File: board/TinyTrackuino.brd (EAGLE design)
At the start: 49.5 x 49.5 mm, 16 parts, among them M2 HX1, Q1 PMV20XN, PMV16UN, etc, U1 LM60 int, X1 BU-SMA-V, X2 Vin, X3 LM60 ext, X4 Buzzer

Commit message: Fixing temp sensor silkscreen and gps connector
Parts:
- moved JP1 2.54 mm to (2.03, 14.7), turned to 90 degrees
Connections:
- net 5V: now also GPSCONN.5; no longer GPSCONN.2
- net GND: now also GPSCONN.6; no longer GPSCONN.1
- net GPSPWRCTRL: now also GPSCONN.1; no longer GPSCONN.6
- net GPSVBAT: now also GPSCONN.2; no longer GPSCONN.5
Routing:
- net GND: track 25.3 -> 54.4 mm, vias 2 -> 1
- net D9: track 52.5 -> 46.0 mm
- net A1: track 25.6 -> 21.0 mm, vias 0 -> 1
- net GPSPWRCTRL: track 12.5 -> 17.1 mm, vias 1 -> 0
- net VIN: track 63.0 -> 59.0 mm
- net 5V: track 44.7 -> 45.7 mm, vias 0 -> 1
- net GPSTX: track 10.6 -> 11.4 mm
- net RESET: track 46.7 -> 47.5 mm
- net GPSVBAT: track 21.0 -> 20.6 mm, vias 1 -> 0
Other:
- board text removed: "HX1"

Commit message: Almost final revision of board
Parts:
- C1, C2: device rcl:E2,5-5 -> adafruit:C3216
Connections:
- net 5V: now also C1.1; no longer C1.+
- net GND: now also C1.2, C2.2; no longer C1.-, C2.-
- net VIN: now also C2.1; no longer C2.+
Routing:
- net GND: track 54.4 -> 19.9 mm, vias 1 -> 3
- net 5V: track 45.7 -> 71.4 mm, vias 1 -> 3
- net D6: track 18.4 -> 25.1 mm, vias 0 -> 1
- net VIN: track 59.0 -> 61.8 mm
- net GPSRX: track 8.78 -> 10.2 mm, vias 0 -> 1
- net N$1: track 16.8 -> 17.7 mm
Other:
- board text removed: "5V"
- board text removed: "GND"

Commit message: Possibly final commit for revision 1
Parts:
- removed GPSCONN: JST, SparkFun-Connectors:EM406
- added X5: SM06B-SRSS-TB, con-jst2:SM06B-SRSS-TB
- C1, C2: device adafruit:C3216 -> SparkFun-Passives:1206
- R1, R2: device resistor:R1206 -> SparkFun-Passives:0603-CAP
- moved R2 2.29 mm to (17.5, 29.2)
- moved C2 1.78 mm to (22.1, 29.2)
- moved R1 1.27 mm to (12.7, 29.2)
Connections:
- net 5V: now also X5.5; no longer GPSCONN.5
- net GND: now also X5.6; no longer GPSCONN.6
- net GPSPWRCTRL: now also X5.1; no longer GPSCONN.1
- net GPSRX: now also X5.4; no longer GPSCONN.4
- net GPSTX: now also X5.3; no longer GPSCONN.3
- net GPSVBAT: now also X5.2; no longer GPSCONN.2
- net RFTX: now also U$2.13; no longer U$2.6
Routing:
- net RFTX: track 3.13 -> 38.8 mm, vias 0 -> 1
- net GPSTX: track 11.4 -> 17.9 mm
- net VIN: track 61.8 -> 56.3 mm, vias 0 -> 2
- net GND: track 19.9 -> 25.3 mm, vias 3 -> 4
- net GPSVBAT: track 20.6 -> 17.3 mm, vias 0 -> 1
- net 5V: track 71.4 -> 74.3 mm, vias 3 -> 2
- net GPSPWRCTRL: track 17.1 -> 15.1 mm, vias 0 -> 1
- net GPSRX: track 10.2 -> 8.46 mm, vias 1 -> 0
- net A2: track 10.8 -> 11.6 mm

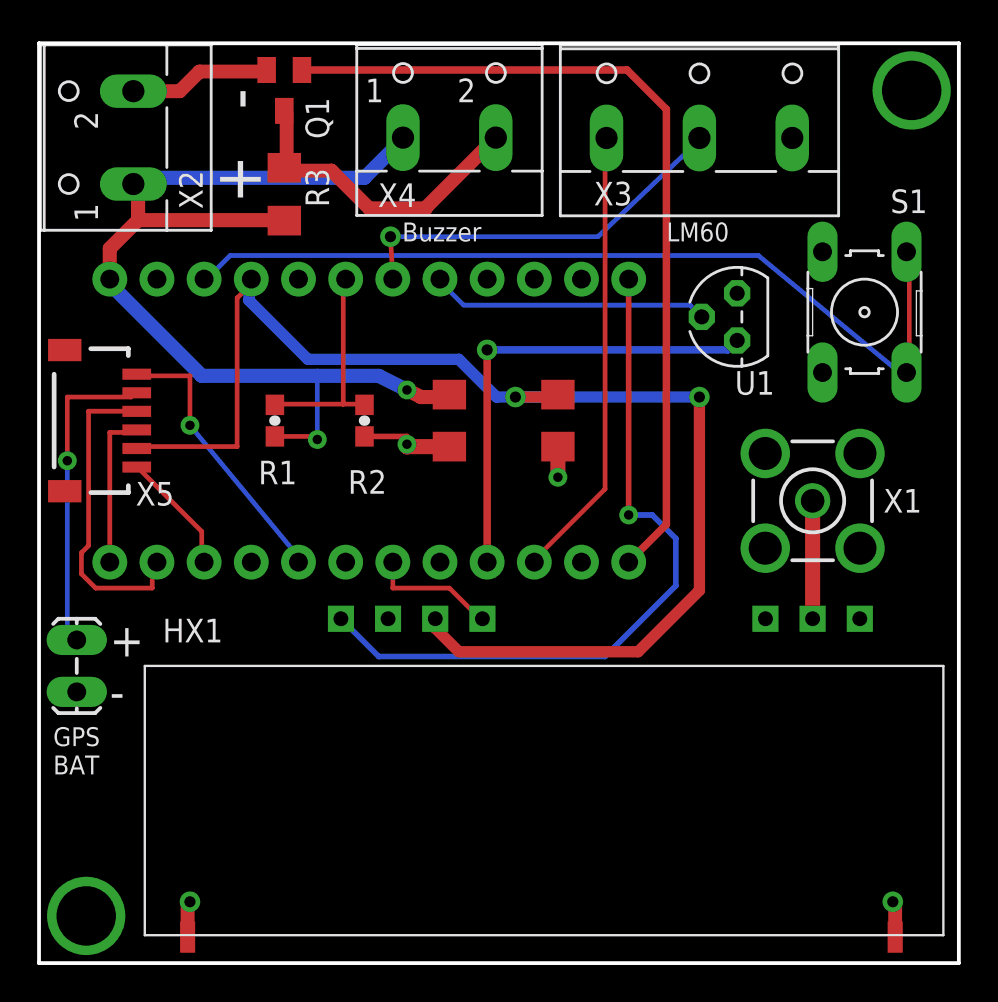
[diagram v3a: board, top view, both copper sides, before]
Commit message: Using 3.5mm screw terminals instead of 5mm
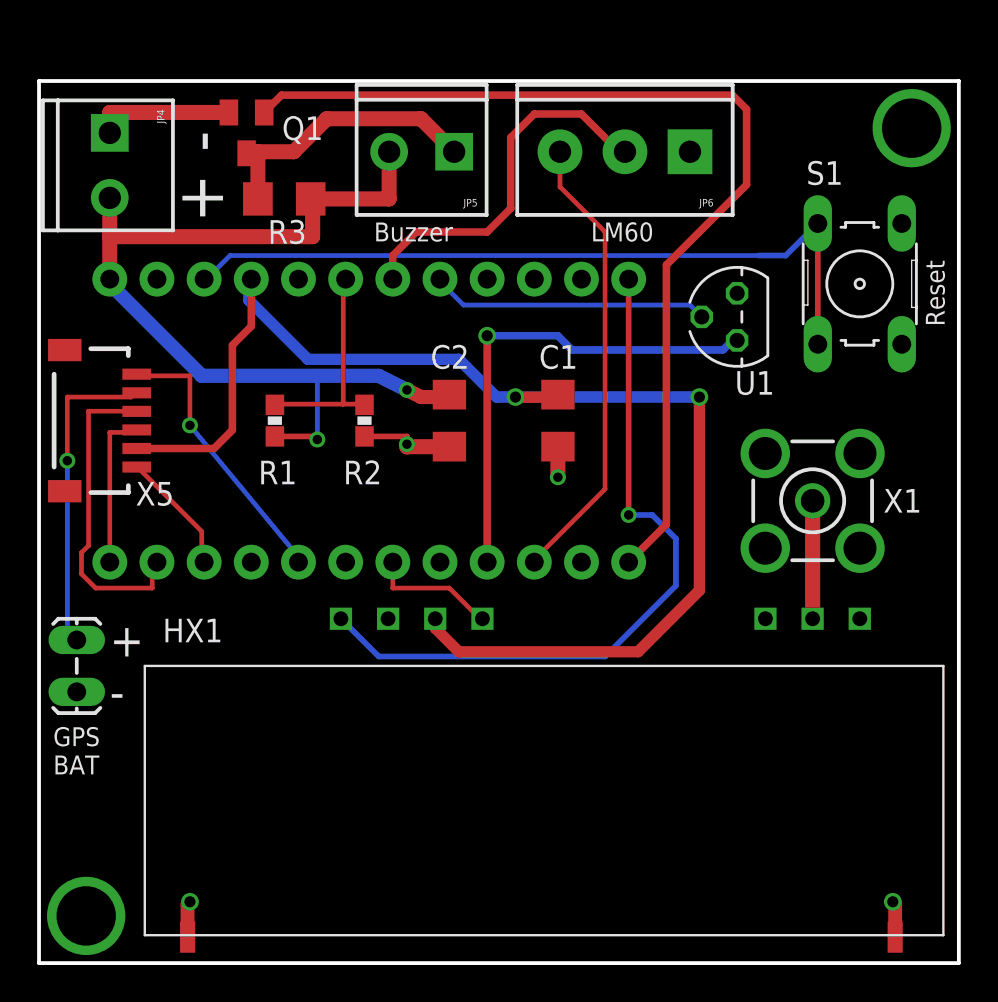
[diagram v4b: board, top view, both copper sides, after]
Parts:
- removed X2: Vin, con-wago-500:W237-102
- removed X3: LM60 ext, con-wago-500:W237-103
- removed X4: Buzzer, con-wago-500:W237-102
- added JP4, JP5: M023.5MM, SparkFun-Connectors:SCREWTERMINAL-3.5MM-2
- added JP6: M033.5MM, SparkFun-Connectors:SCREWTERMINAL-3.5MM-3
- R1, R2: device SparkFun-Passives:0603-CAP -> SparkFun-Passives:0603-RES
- moved Q1 3.06 mm to (11.2, 44.7)
- moved S1 1.55 mm to (44.2, 36.6), turned to 270 degrees
- moved R3 0.25 mm to (13.2, 41.1), turned to 0 degrees
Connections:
- net A1: now also JP6.2; no longer X3.2
- net D7: now also JP6.3; no longer X3.1
- net GND: now also JP4.1, JP6.1; no longer X2.2, X3.3
- net N$1: now also JP5.1; no longer X4.2
- net VIN: now also JP4.2, JP5.2; no longer X2.1, X4.1
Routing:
- net D9: track 45.7 -> 53.7 mm
- net RESET: track 47.2 -> 40.8 mm
- net VIN: track 56.3 -> 50.8 mm
- net N$1: track 17.7 -> 15.3 mm
- net A1: track 21.1 -> 20.0 mm, vias 1 -> 0
- net D6: track 25.1 -> 26.2 mm
- net 5V: track 74.3 -> 73.6 mm
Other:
- board size 49.5 x 49.5 mm -> 49.5 x 47.5 mm
- board text added: "C1"
- board text added: "C2"
- board text added: "Reset"
- board text added: "Tiny Trackuino r1"
- board text added: "~"
- board text removed: "T"
- board text removed: "Tiny Trackuino v1"

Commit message: Moving Vin to edge of board
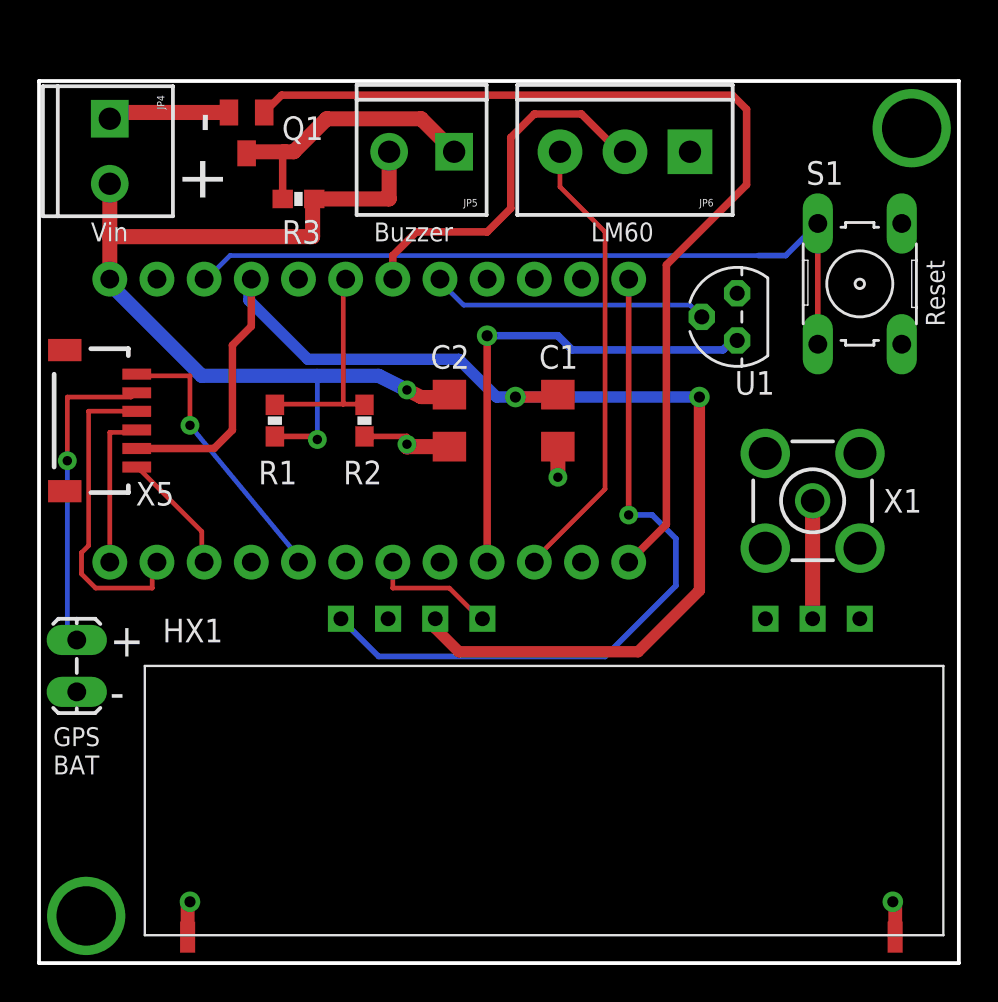
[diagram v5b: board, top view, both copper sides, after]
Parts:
- R3: device resistor:R1206 -> SparkFun-Passives:0603-RES
- moved JP4 0.76 mm to (3.81, 45.5)
- moved R3 0.76 mm to (14.0, 41.1)
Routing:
- net GND: track 25.1 -> 24.4 mm
- net VIN: track 50.8 -> 51.5 mm
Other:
- board text added: "Vin"
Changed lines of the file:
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@@
 <wire x1="0" y1="0" x2="49.53" y2="0" width="0.2032" layer="20"/>
 <wire x1="49.53" y1="0" x2="49.53" y2="47.498" width="0.2032" layer="20"/>
-<text x="9.906" y="43.688" size="2.54" layer="25" rot="R90">-</text>
-<text x="9.906" y="39.878" size="2.54" layer="25" rot="R90">+</text>
+<text x="9.906" y="44.704" size="2.54" layer="25" rot="R90">-</text>
+<text x="9.906" y="40.894" size="2.54" layer="25" rot="R90">+</text>
 <text x="18.034" y="38.862" size="1.016" layer="25">Buzzer</text>
 <text x="29.718" y="38.862" size="1.016" layer="25">LM60</text>
@@
 <text x="19.304" y="45.212" size="1.4224" layer="26" rot="MR0">+</text>
 <text x="22.86" y="45.212" size="1.4224" layer="26" rot="MR0">-</text>
-<text x="2.032" y="40.386" size="1.4224" layer="26" rot="MR0">+</text>
-<text x="2.286" y="45.466" size="1.4224" layer="26" rot="MR270">-</text>
+<text x="2.032" y="41.148" size="1.4224" layer="26" rot="MR0">+</text>
+<text x="2.286" y="46.228" size="1.4224" layer="26" rot="MR270">-</text>
 <text x="38.1" y="3.81" size="2.54" layer="26" rot="MR0">John Boiles</text>
 <text x="3.81" y="16.51" size="1.778" layer="25">+</text>
@@
 <text x="21.082" y="32.004" size="1.27" layer="25">C2</text>
 <text x="26.924" y="32.004" size="1.27" layer="25">C1</text>
+<text x="2.794" y="38.862" size="1.016" layer="25">Vin</text>
 </plain>
 <attributes>
@@
 </class>
 </classes>
-<designrules name="LaenPCBOrder">
-<description language="de">&lt;b&gt;EAGLE Design Rules&lt;/b&gt;
+<designrules name="SparkFun">
+<description language="en">&lt;b&gt;EAGLE Design Rules&lt;/b&gt;
 &lt;p&gt;
-Die Standard-Design-Rules sind so gewählt, dass sie für
-die meisten Anwendungen passen. Sollte ihre Platine
-besondere Anforderungen haben, treffen Sie die erforderlichen
-Einstellungen hier und speichern die Design Rules unter
-einem neuen Namen ab.</description>
-<description language="en">&lt;b&gt;Laen's PCB Order Design Rules&lt;/b&gt;
-&lt;p&gt;
-Please make sure your boards conform to these design rules.</description>
+The default Design Rules have been set to cover
+a wide range of applications. Your particular design
+may have different requirements, so please make the
+necessary adjustments and save your customized
+design rules under a new name.</description>
 <param name="layerSetup" value="(1*16)"/>
-<param name="mtCopper" value="0.0356mm 0.0356mm 0.0356mm 0.0356mm 0.0356mm 0.0356mm 0.0356mm 0.0356mm 0.0356mm 0.0356mm 0.0356mm 0.0356mm 0.0356mm 0.0356mm 0.0356mm 0.0356mm"/>
-<param name="mtIsolate" value="1.5011mm 0.1499mm 0.2007mm 0.1499mm 0.2007mm 0.1499mm 0.2007mm 0.1499mm 0.2007mm 0.1499mm 0.2007mm 0.1499mm 0.2007mm 0.1499mm 0.2007mm"/>
-<param name="mdWireWire" value="6mil"/>
-<param name="mdWirePad" value="6mil"/>
-<param name="mdWireVia" value="6mil"/>
-<param name="mdPadPad" value="6mil"/>
-<param name="mdPadVia" value="6mil"/>
-<param name="mdViaVia" value="6mil"/>
-<param name="mdSmdPad" value="6mil"/>
-<param name="mdSmdVia" value="6mil"/>
-<param name="mdSmdSmd" value="6mil"/>
+<param name="mtCopper" value="0.035mm 0.035mm 0.035mm 0.035mm 0.035mm 0.035mm 0.035mm 0.035mm 0.035mm 0.035mm 0.035mm 0.035mm 0.035mm 0.035mm 0.035mm 0.035mm"/>
+<param name="mtIsolate" value="1.5mm 0.15mm 0.2mm 0.15mm 0.2mm 0.15mm 0.2mm 0.15mm 0.2mm 0.15mm 0.2mm 0.15mm 0.2mm 0.15mm 0.2mm"/>
+<param name="mdWireWire" value="8mil"/>
+<param name="mdWirePad" value="8mil"/>
+<param name="mdWireVia" value="8mil"/>
+<param name="mdPadPad" value="8mil"/>
+<param name="mdPadVia" value="8mil"/>
+<param name="mdViaVia" value="8mil"/>
+<param name="mdSmdPad" value="8mil"/>
+<param name="mdSmdVia" value="8mil"/>
+<param name="mdSmdSmd" value="8mil"/>
 <param name="mdViaViaSameLayer" value="8mil"/>
 <param name="mnLayersViaInSmd" value="2"/>
-<param name="mdCopperDimension" value="15mil"/>
-<param name="mdDrill" value="6mil"/>
+<param name="mdCopperDimension" value="10mil"/>
+<param name="mdDrill" value="8mil"/>
 <param name="mdSmdStop" value="0mil"/>
-<param name="msWidth" value="6mil"/>
-<param name="msDrill" value="13mil"/>
-<param name="msMicroVia" value="13mil"/>
+<param name="msWidth" value="8mil"/>
+<param name="msDrill" value="20mil"/>
+<param name="msMicroVia" value="9.99mm"/>
 <param name="msBlindViaRatio" value="0.5"/>
 <param name="rvPadTop" value="0.25"/>
@@
 <param name="rvMicroViaOuter" value="0.25"/>
 <param name="rvMicroViaInner" value="0.25"/>
-<param name="rlMinPadTop" value="7mil"/>
+<param name="rlMinPadTop" value="12mil"/>
 <param name="rlMaxPadTop" value="20mil"/>
-<param name="rlMinPadInner" value="7mil"/>
+<param name="rlMinPadInner" value="10mil"/>
 <param name="rlMaxPadInner" value="20mil"/>
-<param name="rlMinPadBottom" value="7mil"/>
+<param name="rlMinPadBottom" value="12mil"/>
 <param name="rlMaxPadBottom" value="20mil"/>
-<param name="rlMinViaOuter" value="7mil"/>
+<param name="rlMinViaOuter" value="10mil"/>
 <param name="rlMaxViaOuter" value="20mil"/>
-<param name="rlMinViaInner" value="7mil"/>
+<param name="rlMinViaInner" value="10mil"/>
 <param name="rlMaxViaInner" value="20mil"/>
 <param name="rlMinMicroViaOuter" value="4mil"/>
@@
 <param name="mlMinCreamFrame" value="0mil"/>
 <param name="mlMaxCreamFrame" value="0mil"/>
-<param name="mlViaStopLimit" value="0mil"/>
+<param name="mlViaStopLimit" value="25mil"/>
 <param name="srRoundness" value="0"/>
 <param name="srMinRoundness" value="0mil"/>
@@
 <attribute name="VALUE" x="13.081" y="47.879" size="1.27" layer="27" rot="R180"/>
 </element>
-<element name="R3" library="resistor" package="R1206" value="1K" x="13.208" y="41.148" smashed="yes">
-<attribute name="NAME" x="12.319" y="38.735" size="1.27" layer="25"/>
-<attribute name="VALUE" x="11.811" y="38.735" size="1.27" layer="27"/>
+<element name="R3" library="SparkFun-Passives" package="0603-RES" value="1K" x="13.97" y="41.148" smashed="yes">
+<attribute name="NAME" x="13.081" y="38.735" size="1.27" layer="25"/>
+<attribute name="VALUE" x="12.573" y="38.735" size="1.27" layer="27"/>
 </element>
 <element name="U$2" library="SparkFun-Boards" package="ARDUINO_PRO_MICRO" value="ARDUINO_PRO_MICRO" x="16.51" y="29.21" smashed="yes" rot="R90">
@@
 <attribute name="VALUE" x="0.381" y="22.86" size="1.27" layer="27"/>
 </element>
-<element name="JP4" library="SparkFun-Connectors" package="SCREWTERMINAL-3.5MM-2" value="M023.5MM" x="3.81" y="44.704" rot="R270"/>
+<element name="JP4" library="SparkFun-Connectors" package="SCREWTERMINAL-3.5MM-2" value="M023.5MM" x="3.81" y="45.466" rot="R270"/>
 <element name="JP5" library="SparkFun-Connectors" package="SCREWTERMINAL-3.5MM-2" value="M023.5MM" x="22.352" y="43.688" rot="R180"/>
 <element name="JP6" library="SparkFun-Connectors" package="SCREWTERMINAL-3.5MM-3" value="M033.5MM" x="35.052" y="43.688" rot="R180"/>
@@
 <contactref element="JP6" pad="1"/>
 <wire x1="10.226" y1="45.804" x2="3.81" y2="45.804" width="0.8128" layer="1"/>
-<wire x1="3.81" y1="45.804" x2="3.81" y2="44.704" width="0.8128" layer="1"/>
+<wire x1="3.81" y1="45.804" x2="3.81" y2="45.466" width="0.8128" layer="1"/>
 </signal>
 <signal name="VIN">
@@
 <contactref element="JP4" pad="2"/>
 <wire x1="3.81" y1="36.83" x2="3.81" y2="39.116" width="0.8128" layer="1"/>
-<wire x1="3.81" y1="39.116" x2="3.81" y2="41.204" width="0.8128" layer="1"/>
-<wire x1="14.63" y1="41.148" x2="14.732" y2="41.148" width="0.8128" layer="1"/>
+<wire x1="3.81" y1="39.116" x2="3.81" y2="41.966" width="0.8128" layer="1"/>
+<wire x1="14.82" y1="41.148" x2="14.732" y2="41.148" width="0.8128" layer="1"/>
 <wire x1="18.852" y1="41.148" x2="18.852" y2="43.688" width="0.8128" layer="1"/>
-<wire x1="18.852" y1="41.148" x2="14.732" y2="41.148" width="0.8128" layer="1"/>
+<wire x1="18.852" y1="41.148" x2="14.82" y2="41.148" width="0.8128" layer="1"/>
 <wire x1="14.732" y1="41.148" x2="14.732" y2="39.116" width="0.8128" layer="1"/>
 <wire x1="14.732" y1="39.116" x2="3.81" y2="39.116" width="0.8128" layer="1"/>
@@
 <contactref element="JP5" pad="1"/>
 <wire x1="11.176" y1="43.688" x2="11.176" y2="43.604" width="0.8128" layer="1"/>
-<wire x1="11.176" y1="43.688" x2="11.786" y2="43.688" width="0.8128" layer="1"/>
-<wire x1="11.786" y1="43.688" x2="11.786" y2="41.148" width="0.8128" layer="1"/>
-<wire x1="11.786" y1="43.688" x2="13.716" y2="43.688" width="0.8128" layer="1"/>
+<wire x1="11.176" y1="43.688" x2="13.208" y2="43.688" width="0.8128" layer="1"/>
+<wire x1="13.208" y1="43.688" x2="13.716" y2="43.688" width="0.8128" layer="1"/>
 <wire x1="13.716" y1="43.688" x2="15.494" y2="45.466" width="0.8128" layer="1"/>
 <wire x1="15.494" y1="45.466" x2="20.574" y2="45.466" width="0.8128" layer="1"/>
 <wire x1="20.574" y1="45.466" x2="22.352" y2="43.688" width="0.8128" layer="1"/>
+<wire x1="13.12" y1="41.148" x2="13.12" y2="43.6" width="0.4064" layer="1"/>
+<wire x1="13.12" y1="43.6" x2="13.208" y2="43.688" width="0.4064" layer="1"/>
 </signal>
 <signal name="N$3">
